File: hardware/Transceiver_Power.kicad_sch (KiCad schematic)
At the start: 31 parts, among them U3 AD9361

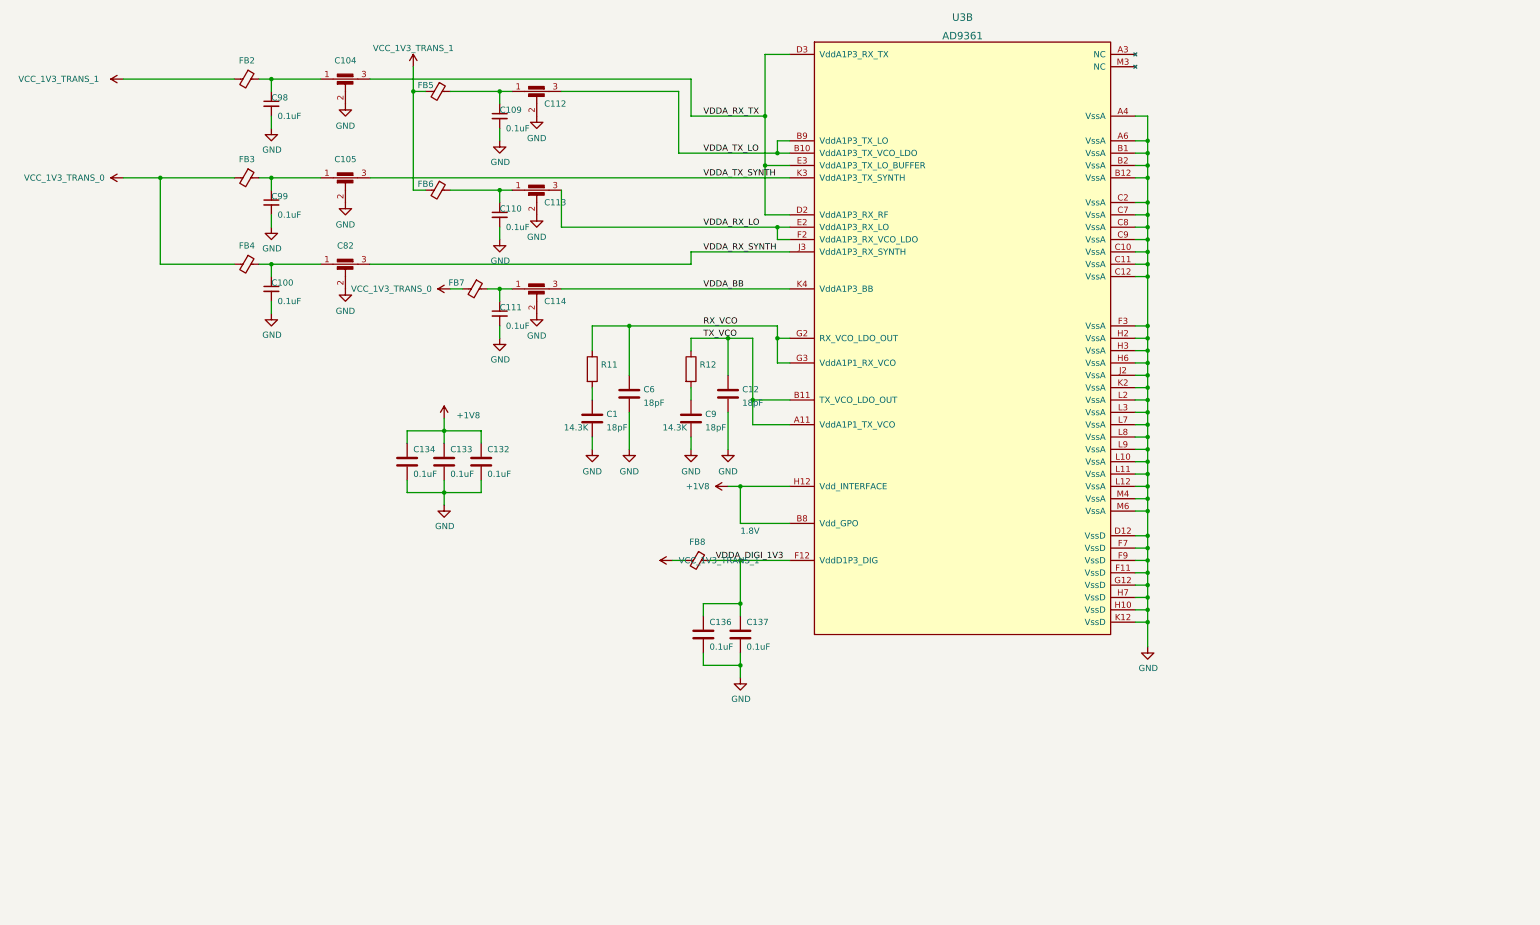
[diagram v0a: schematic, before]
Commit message: add sdio level shift ciruit
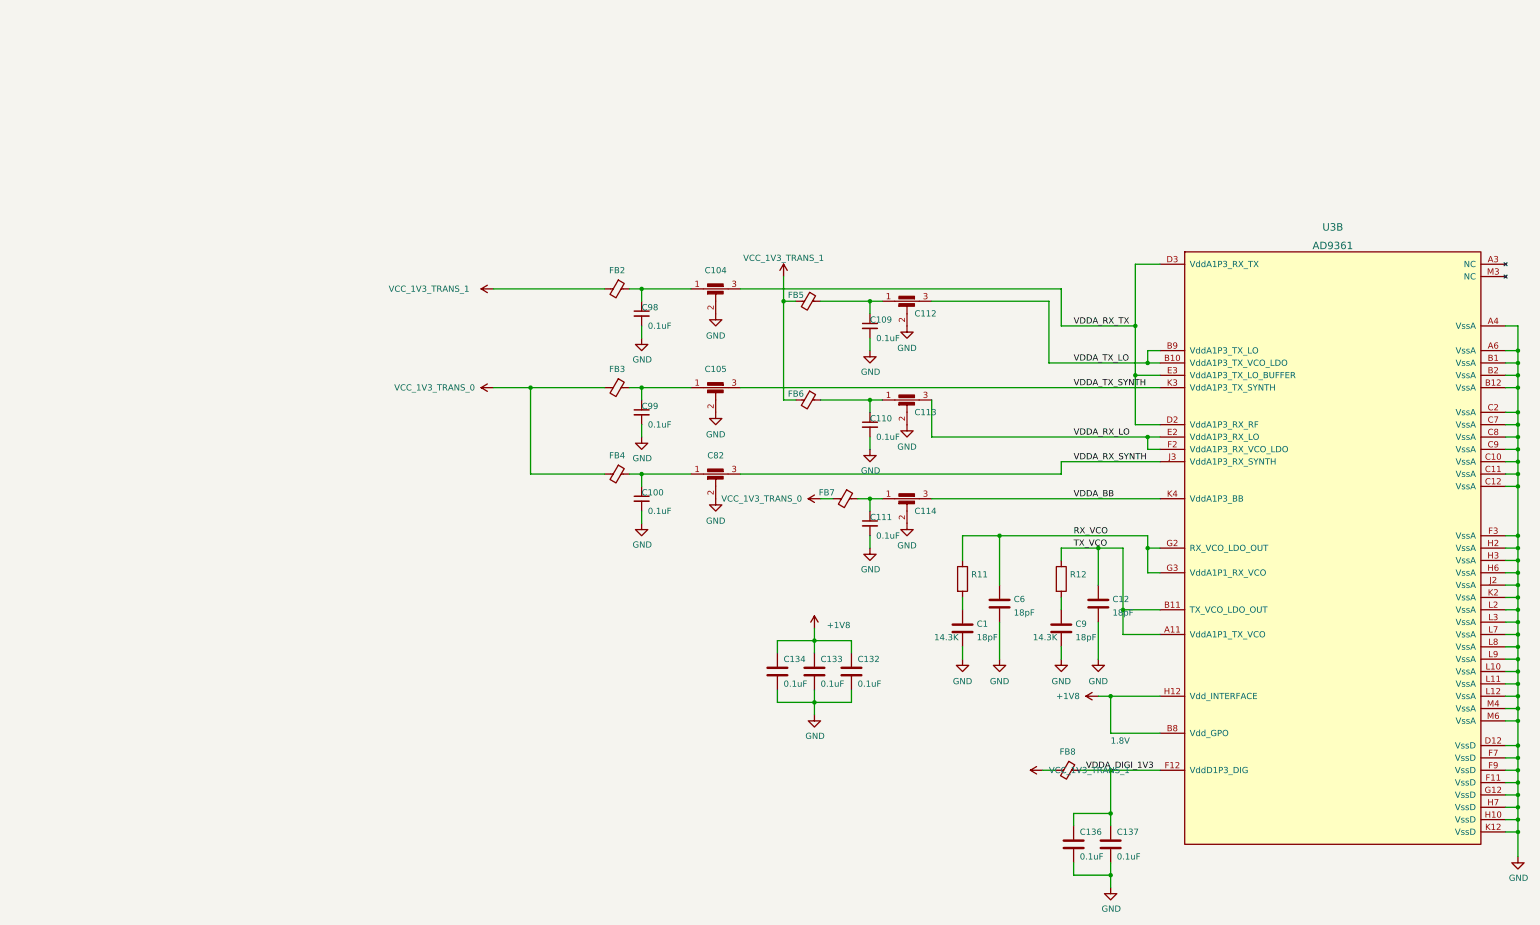
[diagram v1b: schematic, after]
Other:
- moved on the sheet: C1, C100, C104, C105, C109, C110, C111, C112, C113, C114, C12, C132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
